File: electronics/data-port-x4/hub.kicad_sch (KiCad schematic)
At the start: 31 parts, among them J1 LEAD, U1 USB2514B-AEZC-TR, U2 TCA6408ARGTR, U3 AP2112K-3.3TRG1, U4 USBLC6-2SC6, U5 USBLC6-2SC6, U6 TCA6408ARGTR, Y1 X322524MSB4SI

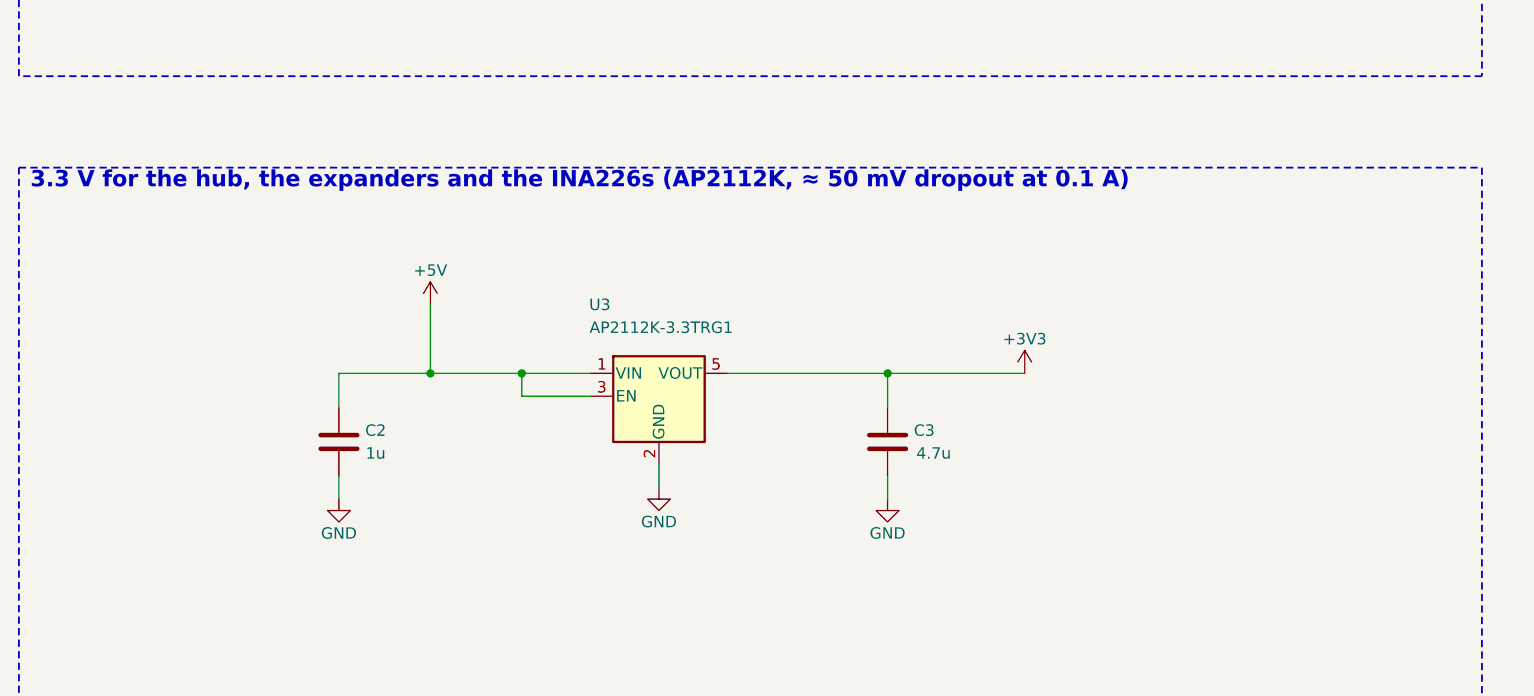
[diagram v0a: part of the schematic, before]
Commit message: DATA ×4: a basic-part LDO, the XC6206 in U3's spot
U3 goes from the AP2112K-3.3 (extended) to the XC6206P332MR-G (C5446,
JLC basic, SOT-23-3): one extended part type fewer, $3.07 an order at
Economic PCBA.  Its dropout is ≈ 0.25 V at 0.1 A against the board's
≈ 0.1 A of logic, so the hub, the expanders and the INA226s still run
down to ≈ 3.6 V in; 200 mA max, 6 V in max (the node's +5V is 5.24 V).
The AMS1117 suggested first doesn't fit (SOT-223 under J1) and its ≈ 1 V
dropout would eat the lead's margin.  U3 sits at 0° (of three
orientations routed, the one Freerouting closed), CPL fix 180° for
C5446.

Re-routed: ERC 0, DRC 0 (unconnected 0, parity 0).  BOM: the DATA ×4
quote at 8 extended types ($74.44), its lever moves out of JLC_LEVERS.

Co-Authored-By: Claude Opus 5.5 <noreply@anthropic.com>
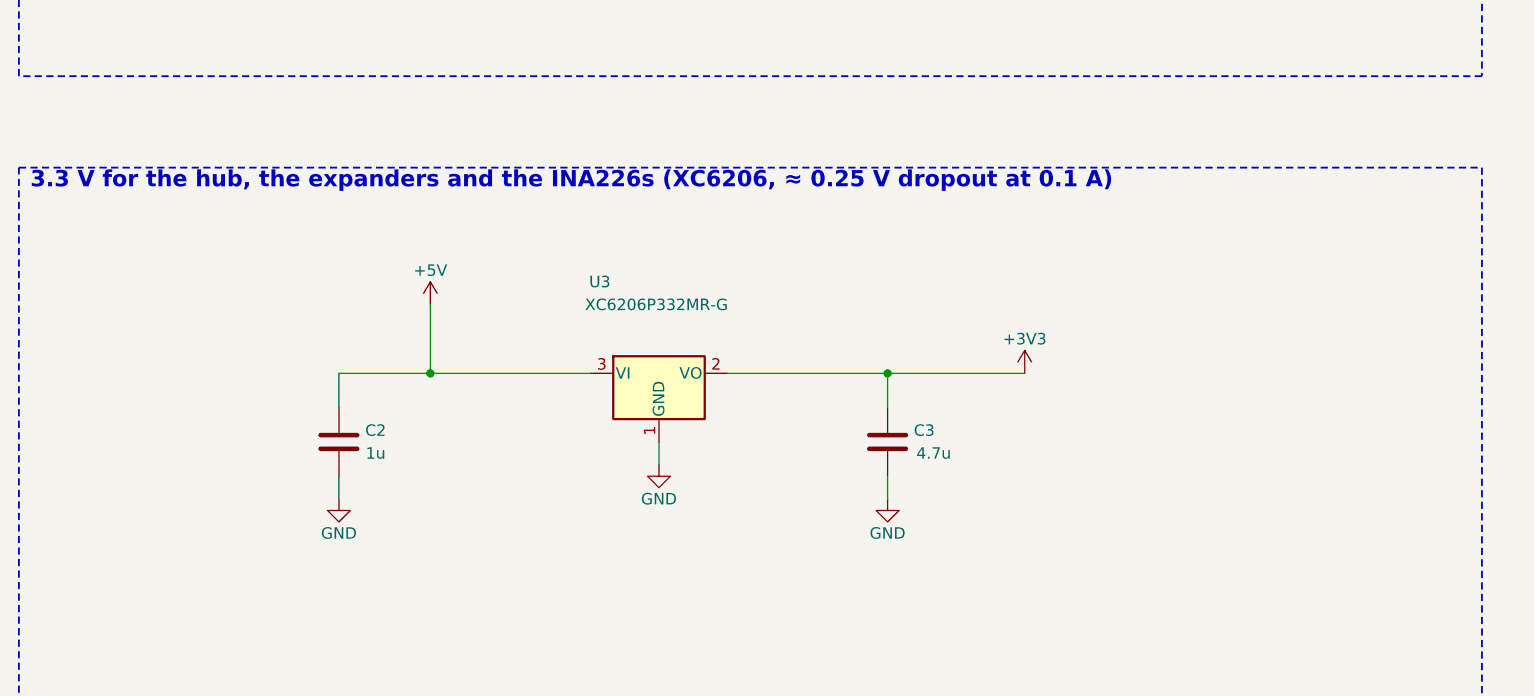
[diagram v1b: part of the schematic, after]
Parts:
- U3: value AP2112K-3.3TRG1 -> XC6206P332MR-G; footprint Package_TO_SOT_SMD:SOT-23-5 -> Package_TO_SOT_SMD:SOT-23-3; symbol Regulator_Linear:AP2112K-3.3 -> Regulator_Linear:XC6206PxxxMR; LCSC C51118 -> C5446; MPN AP2112K-3.3TRG1 -> XC6206P332MR-G; Manufacturer Diodes Incorporated -> Torex Semicon
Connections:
- net +3V3: now also U3.2 (VO); no longer U3.5 (VOUT)
- net +5V: no longer U3.1 (VIN)
- net GND: now also U3.1 (GND); no longer U3.2 (GND)
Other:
- note added: "3.3 V for the hub, the expanders and the INA226s (XC6206, ≈ 0.25 V dropout at 0.1 A)"
- note removed: "3.3 V for the hub, the expanders and the INA226s (AP2112K, ≈ 50 mV dropout at 0.1 A)"
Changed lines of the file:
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@@
 	)
 	(symbol
-		(lib_id "Regulator_Linear:AP2112K-3.3")
-		(at 86.36 177.8 0)
+		(lib_id "Regulator_Linear:XC6206PxxxMR")
+		(at 86.36 175.26 0)
 		(unit 1)
 		(exclude_from_sim no)
@@
 		(fields_autoplaced yes)
 		(property "Reference" "U3"
-			(at 79.79 167.64 0)
+			(at 79.79 165.1 0)
 			(effects
 				(font
@@
 			)
 		)
-		(property "Value" "AP2112K-3.3TRG1"
-			(at 86.615 170.18 0)
+		(property "Value" "XC6206P332MR-G"
+			(at 86.09 167.64 0)
 			(effects
 				(font
@@
 			)
 		)
-		(property "Footprint" "Package_TO_SOT_SMD:SOT-23-5"
-			(at 86.36 177.8 0)
+		(property "Footprint" "Package_TO_SOT_SMD:SOT-23-3"
+			(at 86.36 175.26 0)
 			(effects
 				(font
@@
 			)
 		)
-		(property "Datasheet" ""
-			(at 86.36 177.8 0)
+		(property "Datasheet" "https://www.lcsc.com/datasheet/lcsc_datasheet_2304140030_Torex-Semicon-XC6206P332MR-G_C5446.pdf"
+			(at 86.36 175.26 0)
 			(effects
 				(font
@@
 			)
 		)
-		(property "Description" "3.3 V 600 mA LDO, 250 mV dropout"
-			(at 86.36 177.8 0)
+		(property "Description" "3.3 V 200 mA LDO, ≈ 0.25 V dropout at 100 mA, 6 V max in"
+			(at 86.36 175.26 0)
 			(effects
 				(font
@@
 			)
 		)
-		(property "MPN" "AP2112K-3.3TRG1"
-			(at 86.36 177.8 0)
+		(property "MPN" "XC6206P332MR-G"
+			(at 86.36 175.26 0)
 			(effects
 				(font
@@
 			)
 		)
-		(property "Manufacturer" "Diodes Incorporated"
-			(at 86.36 177.8 0)
+		(property "Manufacturer" "Torex Semicon"
+			(at 86.36 175.26 0)
 			(effects
 				(font
@@
 			)
 		)
-		(property "LCSC" "C51118"
-			(at 86.36 177.8 0)
+		(property "LCSC" "C5446"
+			(at 86.36 175.26 0)
 			(effects
 				(font
@@
 		(pin "3"
 		)
-		(pin "4"
-		)
-		(pin "5"
-		)
 		(instances
 			(project "data-port-x4"
@@
 	(wire
 		(pts
+			(xy 86.36 182.88)
 			(xy 86.36 185.42)
-			(xy 86.36 187.96)
 		)
 		(stroke
@@
 	(symbol
 		(lib_id "power:GND")
-		(at 86.36 187.96 0)
+		(at 86.36 185.42 0)
 		(unit 1)
 		(exclude_from_sim no)
@@
 		(fields_autoplaced yes)
 		(property "Reference" "#PWR02012"
-			(at 86.36 187.96 0)
+			(at 86.36 185.42 0)
 			(effects
 				(font
@@
 		)
 		(property "Value" "GND"
-			(at 86.36 191.77 0)
+			(at 86.36 189.23 0)
 			(effects
 				(font
@@
 		)
 		(property "Footprint" ""
-			(at 86.36 187.96 0)
+			(at 86.36 185.42 0)
 			(effects
 				(font
@@
 		)
 		(property "Datasheet" ""
-			(at 86.36 187.96 0)
+			(at 86.36 185.42 0)
 			(effects
 				(font
@@
 		)
 		(property "Description" ""
-			(at 86.36 187.96 0)
+			(at 86.36 185.42 0)
 			(effects
 				(font
@@
 	(wire
 		(pts
-			(xy 78.74 177.8)
-			(xy 71.12 177.8)
-		)
-		(stroke
-			(width 0)
-			(type default)
-		)
-	)
-	(wire
-		(pts
-			(xy 71.12 177.8)
-			(xy 71.12 175.26)
-		)
-		(stroke
-			(width 0)
-			(type default)
-		)
-	)
-	(wire
-		(pts
 			(xy 93.98 175.26)
 			(xy 111.76 175.26)
@@
 	)
 	(junction
-		(at 71.12 175.26)
-		(diameter 0)
-		(color 0 0 0 0)
-	)
-	(junction
 		(at 111.76 175.26)
 		(diameter 0)
@@
 		)
 	)
-	(text "3.3 V for the hub, the expanders and the INA226s (AP2112K, ≈ 50 mV dropout at 0.1 A)"
+	(text "3.3 V for the hub, the expanders and the INA226s (XC6206, ≈ 0.25 V dropout at 0.1 A)"
 		(exclude_from_sim no)
 		(at 16.51 154.94 0)

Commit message: DATA ×4: back to the AP2112K on U3, on top-side copper
The XC6206 (82c7172) can't carry this rail.  The USB2514B alone draws up
to 155 mA at high speed with four ports busy (datasheet tables 6-4 and
6-5; 84 mA at full speed), so the LDO burns ≈ 0.31 W from 5.24 V: more
than a 200 mA SOT-23 LDO like the XC6206 is rated for (≈ 0.25 W), and the
XC6206 has no thermal shutdown.  The AP2112K-3.3 (600 mA, thermal
shutdown) is back on its SOT-23-5 footprint at 0°, CPL 270° as before;
C5446 and its catalog entry go.

Its VIN and EN pins (with C2's +5V pad) and its GND pin now sit on
top-side islands (exclusive, thermal reliefs) with their own vias to the
+5V and GND planes, to spread that heat.  design.py and docs/electronics.md
say why, so it isn't swapped again.

Re-routed: ERC 0, DRC 0 (unconnected 0, parity 0).  BOM: back to 9
extended types, the DATA ×4 order $103.76.

Co-Authored-By: Claude Opus 5.5 <noreply@anthropic.com>
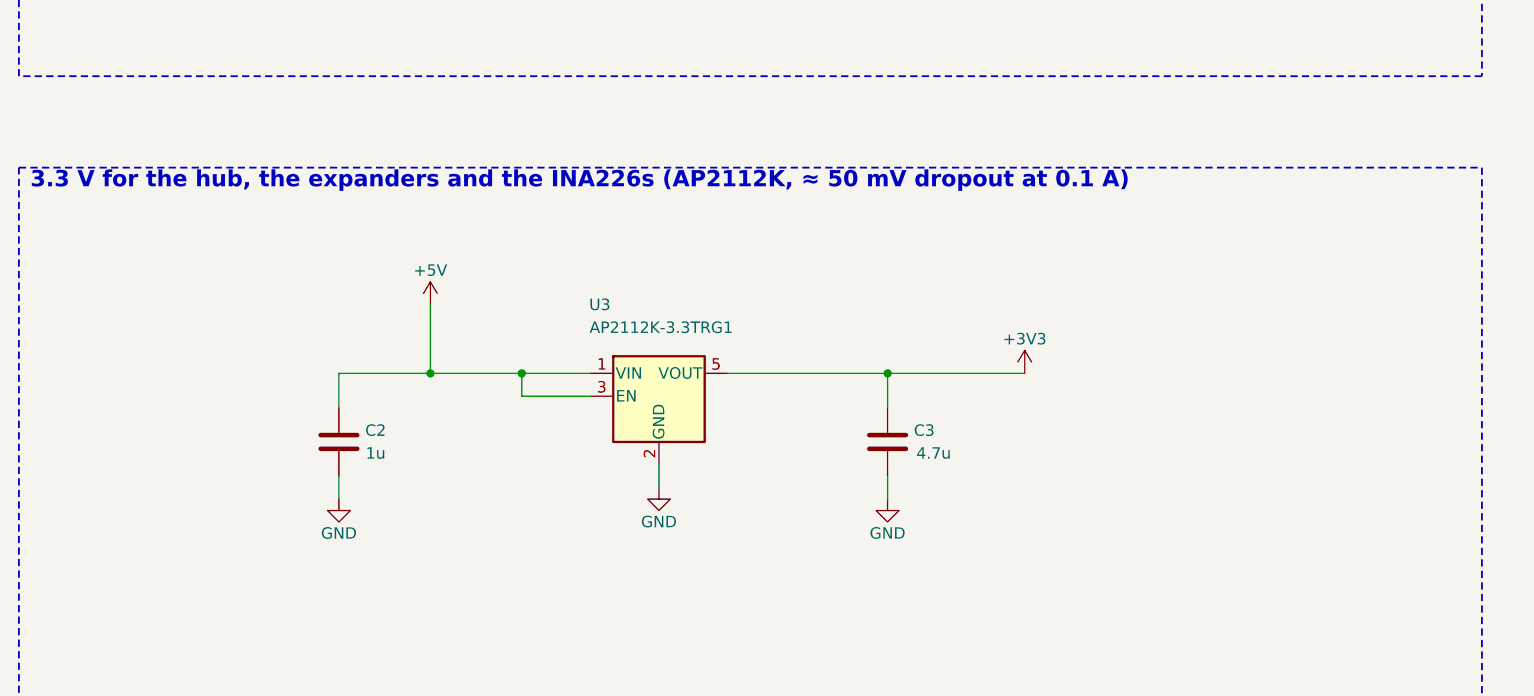
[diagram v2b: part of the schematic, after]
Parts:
- U3: value XC6206P332MR-G -> AP2112K-3.3TRG1; footprint Package_TO_SOT_SMD:SOT-23-3 -> Package_TO_SOT_SMD:SOT-23-5; symbol Regulator_Linear:XC6206PxxxMR -> Regulator_Linear:AP2112K-3.3; LCSC C5446 -> C51118; MPN XC6206P332MR-G -> AP2112K-3.3TRG1; Manufacturer Torex Semicon -> Diodes Incorporated
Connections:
- net +3V3: now also U3.5 (VOUT); no longer U3.2 (VO)
- net +5V: now also U3.1 (VIN)
- net GND: now also U3.2 (GND); no longer U3.1 (GND)
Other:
- note added: "3.3 V for the hub, the expanders and the INA226s (AP2112K, ≈ 50 mV dropout at 0.1 A)"
- note removed: "3.3 V for the hub, the expanders and the INA226s (XC6206, ≈ 0.25 V dropout at 0.1 A)"
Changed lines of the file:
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@@
 	)
 	(symbol
-		(lib_id "Regulator_Linear:XC6206PxxxMR")
-		(at 86.36 175.26 0)
+		(lib_id "Regulator_Linear:AP2112K-3.3")
+		(at 86.36 177.8 0)
 		(unit 1)
 		(exclude_from_sim no)
@@
 		(fields_autoplaced yes)
 		(property "Reference" "U3"
-			(at 79.79 165.1 0)
+			(at 79.79 167.64 0)
 			(effects
 				(font
@@
 			)
 		)
-		(property "Value" "XC6206P332MR-G"
-			(at 86.09 167.64 0)
+		(property "Value" "AP2112K-3.3TRG1"
+			(at 86.615 170.18 0)
 			(effects
 				(font
@@
 			)
 		)
-		(property "Footprint" "Package_TO_SOT_SMD:SOT-23-3"
-			(at 86.36 175.26 0)
+		(property "Footprint" "Package_TO_SOT_SMD:SOT-23-5"
+			(at 86.36 177.8 0)
 			(effects
 				(font
@@
 			)
 		)
-		(property "Datasheet" "https://www.lcsc.com/datasheet/lcsc_datasheet_2304140030_Torex-Semicon-XC6206P332MR-G_C5446.pdf"
-			(at 86.36 175.26 0)
+		(property "Datasheet" ""
+			(at 86.36 177.8 0)
 			(effects
 				(font
@@
 			)
 		)
-		(property "Description" "3.3 V 200 mA LDO, ≈ 0.25 V dropout at 100 mA, 6 V max in"
-			(at 86.36 175.26 0)
+		(property "Description" "3.3 V 600 mA LDO, 250 mV dropout"
+			(at 86.36 177.8 0)
 			(effects
 				(font
@@
 			)
 		)
-		(property "MPN" "XC6206P332MR-G"
-			(at 86.36 175.26 0)
+		(property "MPN" "AP2112K-3.3TRG1"
+			(at 86.36 177.8 0)
 			(effects
 				(font
@@
 			)
 		)
-		(property "Manufacturer" "Torex Semicon"
-			(at 86.36 175.26 0)
+		(property "Manufacturer" "Diodes Incorporated"
+			(at 86.36 177.8 0)
 			(effects
 				(font
@@
 			)
 		)
-		(property "LCSC" "C5446"
-			(at 86.36 175.26 0)
+		(property "LCSC" "C51118"
+			(at 86.36 177.8 0)
 			(effects
 				(font
@@
 		(pin "3"
 		)
+		(pin "4"
+		)
+		(pin "5"
+		)
 		(instances
 			(project "data-port-x4"
@@
 	(wire
 		(pts
-			(xy 86.36 182.88)
 			(xy 86.36 185.42)
+			(xy 86.36 187.96)
 		)
 		(stroke
@@
 	(symbol
 		(lib_id "power:GND")
-		(at 86.36 185.42 0)
+		(at 86.36 187.96 0)
 		(unit 1)
 		(exclude_from_sim no)
@@
 		(fields_autoplaced yes)
 		(property "Reference" "#PWR02012"
-			(at 86.36 185.42 0)
+			(at 86.36 187.96 0)
 			(effects
 				(font
@@
 		)
 		(property "Value" "GND"
-			(at 86.36 189.23 0)
+			(at 86.36 191.77 0)
 			(effects
 				(font
@@
 		)
 		(property "Footprint" ""
-			(at 86.36 185.42 0)
+			(at 86.36 187.96 0)
 			(effects
 				(font
@@
 		)
 		(property "Datasheet" ""
-			(at 86.36 185.42 0)
+			(at 86.36 187.96 0)
 			(effects
 				(font
@@
 		)
 		(property "Description" ""
-			(at 86.36 185.42 0)
+			(at 86.36 187.96 0)
 			(effects
 				(font
@@
 	(wire
 		(pts
+			(xy 78.74 177.8)
+			(xy 71.12 177.8)
+		)
+		(stroke
+			(width 0)
+			(type default)
+		)
+	)
+	(wire
+		(pts
+			(xy 71.12 177.8)
+			(xy 71.12 175.26)
+		)
+		(stroke
+			(width 0)
+			(type default)
+		)
+	)
+	(wire
+		(pts
 			(xy 93.98 175.26)
 			(xy 111.76 175.26)
@@
 	)
 	(junction
+		(at 71.12 175.26)
+		(diameter 0)
+		(color 0 0 0 0)
+	)
+	(junction
 		(at 111.76 175.26)
 		(diameter 0)
@@
 		)
 	)
-	(text "3.3 V for the hub, the expanders and the INA226s (XC6206, ≈ 0.25 V dropout at 0.1 A)"
+	(text "3.3 V for the hub, the expanders and the INA226s (AP2112K, ≈ 50 mV dropout at 0.1 A)"
 		(exclude_from_sim no)
 		(at 16.51 154.94 0)
